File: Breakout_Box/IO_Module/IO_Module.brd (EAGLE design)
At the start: 64 x 35 mm, 5 parts, among them U1 AGND, U2 AGND, U3 AGND

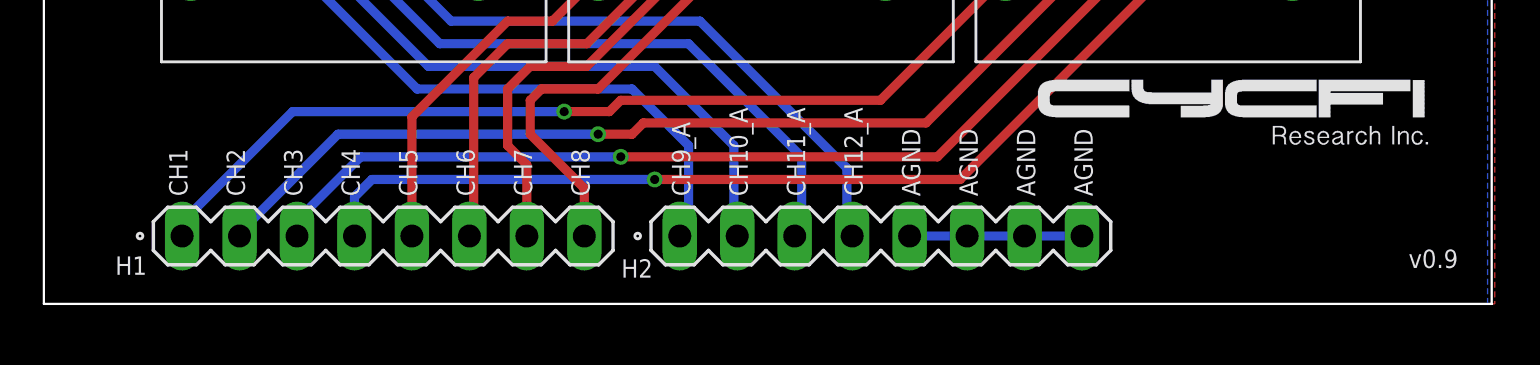
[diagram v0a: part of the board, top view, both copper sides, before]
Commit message: Update: Main Board MIDI Board MCU Board IO Board
Delete:
Mixer Board
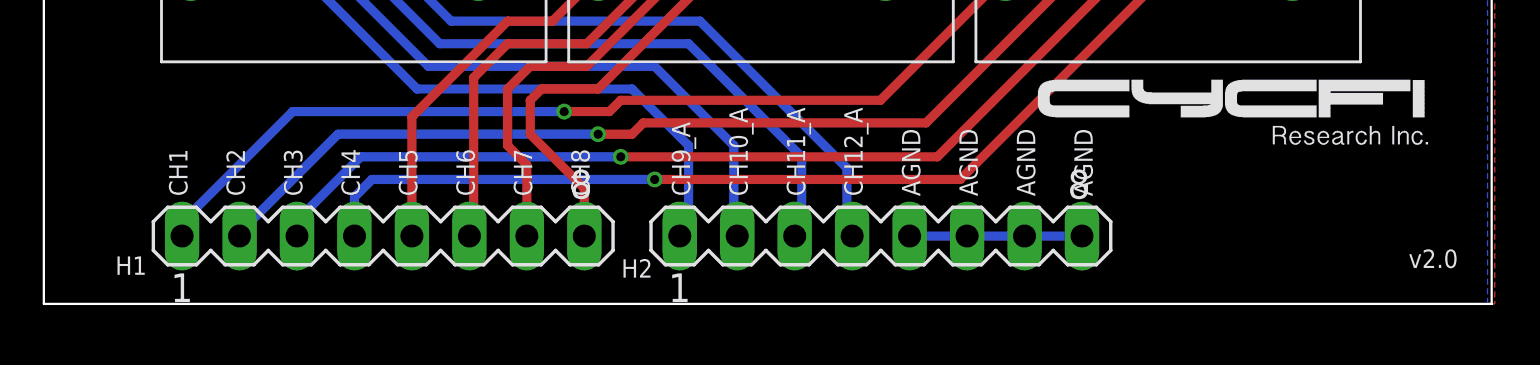
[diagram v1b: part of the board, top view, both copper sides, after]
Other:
- board text added: "v2.0"
- board text removed: "v0.9"
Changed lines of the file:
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@@
 <?xml version="1.0" encoding="utf-8"?>
 <!DOCTYPE eagle SYSTEM "eagle.dtd">
-<eagle version="6.3">
+<eagle version="9.0.0">
 <drawing>
 <settings>
-<setting alwaysvectorfont="yes"/>
+<setting alwaysvectorfont="no"/>
+<setting keepoldvectorfont="yes"/>
 <setting verticaltext="up"/>
 </settings>
@@
 <layer number="59" name="tCarbon" color="7" fill="1" visible="no" active="no"/>
 <layer number="60" name="bCarbon" color="7" fill="1" visible="no" active="no"/>
-<layer number="90" name="Modules" color="5" fill="1" visible="yes" active="yes"/>
+<layer number="90" name="Modules" color="5" fill="1" visible="no" active="no"/>
 <layer number="91" name="Nets" color="2" fill="1" visible="no" active="no"/>
 <layer number="92" name="Busses" color="1" fill="1" visible="no" active="no"/>
@@
 <text x="43.8242" y="4.7611" size="0.8128" layer="25" ratio="10" rot="R90">AGND</text>
 <text x="46.3642" y="4.7611" size="0.8128" layer="25" ratio="10" rot="R90">AGND</text>
-<text x="60.325" y="1.5875" size="0.8128" layer="25" ratio="10">v0.9</text>
+<text x="60.325" y="1.5875" size="0.8128" layer="25" ratio="10">v2.0</text>
 <rectangle x1="55.249190625" y1="7.03266875" x2="55.391428125" y2="7.05045" layer="25"/>
 <rectangle x1="55.853709375" y1="7.03266875" x2="56.013728125" y2="7.05045" layer="25"/>
@@
 <text x="43.8242" y="4.7611" size="0.8128" layer="125" ratio="10" rot="R90">AGND</text>
 <text x="46.3642" y="4.7611" size="0.8128" layer="125" ratio="10" rot="R90">AGND</text>
-<text x="60.325" y="1.5875" size="0.8128" layer="125" ratio="10">v0.9</text>
+<text x="60.325" y="1.5875" size="0.8128" layer="125" ratio="10">v2.0</text>
 <rectangle x1="55.249190625" y1="7.03266875" x2="55.391428125" y2="7.05045" layer="125"/>
 <rectangle x1="55.853709375" y1="7.03266875" x2="56.013728125" y2="7.05045" layer="125"/>
@@
 <param name="dpMaxLengthDifference" value="10mm"/>
 <param name="dpGapFactor" value="2.5"/>
-<param name="checkGrid" value="0"/>
 <param name="checkAngle" value="0"/>
 <param name="checkFont" value="1"/>
 <param name="checkRestrict" value="0"/>
+<param name="checkStop" value="0"/>
+<param name="checkValues" value="0"/>
 <param name="useDiameter" value="13"/>
 <param name="maxErrors" value="50"/>
@@
 <pass name="Default">
 <param name="RoutingGrid" value="50mil"/>
+<param name="AutoGrid" value="1"/>
+<param name="Efforts" value="0"/>
+<param name="TopRouterVariant" value="1"/>
 <param name="tpViaShape" value="round"/>
 <param name="PrefDir.1" value="|"/>
@@
 </autorouter>
 <elements>
-<element name="H2" library="con-lstb" package="MA08-1" value="" x="37" y="3" smashed="yes">
+<element name="H2" library="con-lstb" library_urn="urn:adsk.eagle:library:162" package="MA08-1" package3d_urn="urn:adsk.eagle:package:8343/1" value="" x="37" y="3" smashed="yes">
+<attribute name="MF" value="" x="61.13" y="-54.15" size="1.778" layer="27" display="off"/>
+<attribute name="MPN" value="" x="61.13" y="-54.15" size="1.778" layer="27" display="off"/>
+<attribute name="NAME" x="25.5225" y="1.1585" size="0.8128" layer="25" ratio="10"/>
+<attribute name="OC_FARNELL" value="unknown" x="61.13" y="-54.15" size="1.778" layer="27" display="off"/>
 <attribute name="OC_NEWARK" value="unknown" x="61.13" y="-54.15" size="1.778" layer="27" display="off"/>
-<attribute name="MPN" value="" x="61.13" y="-54.15" size="1.778" layer="27" display="off"/>
-<attribute name="MF" value="" x="61.13" y="-54.15" size="1.778" layer="27" display="off"/>
-<attribute name="OC_FARNELL" value="unknown" x="61.13" y="-54.15" size="1.778" layer="27" display="off"/>
-<attribute name="NAME" x="25.5225" y="1.1585" size="0.8128" layer="25" ratio="10"/>
 <attribute name="VALUE" x="35.73" y="0.079" size="1.27" layer="27" ratio="10"/>
 </element>
-<element name="H1" library="con-lstb" package="MA08-1" value="" x="15" y="3" smashed="yes">
+<element name="H1" library="con-lstb" library_urn="urn:adsk.eagle:library:162" package="MA08-1" package3d_urn="urn:adsk.eagle:package:8343/1" value="" x="15" y="3" smashed="yes">
+<attribute name="MF" value="" x="60.72" y="-54.15" size="1.778" layer="27" display="off"/>
+<attribute name="MPN" value="" x="60.72" y="-54.15" size="1.778" layer="27" display="off"/>
+<attribute name="NAME" x="3.1575" y="1.286" size="0.8128" layer="25" ratio="10"/>
+<attribute name="OC_FARNELL" value="unknown" x="60.72" y="-54.15" size="1.778" layer="27" display="off"/>
 <attribute name="OC_NEWARK" value="unknown" x="60.72" y="-54.15" size="1.778" layer="27" display="off"/>
-<attribute name="MPN" value="" x="60.72" y="-54.15" size="1.778" layer="27" display="off"/>
-<attribute name="MF" value="" x="60.72" y="-54.15" size="1.778" layer="27" display="off"/>
-<attribute name="OC_FARNELL" value="unknown" x="60.72" y="-54.15" size="1.778" layer="27" display="off"/>
-<attribute name="NAME" x="3.1575" y="1.286" size="0.8128" layer="25" ratio="10"/>
 <attribute name="VALUE" x="13.73" y="0.079" size="1.27" layer="27" ratio="10"/>
 </element>
@@
 </board>
 </drawing>
+<compatibility>
+<note version="8.2" severity="warning">
+Since Version 8.2, EAGLE supports online libraries. The ids
+of those online libraries will not be understood (or retained)
+with this version.
+</note>
+<note version="8.3" severity="warning">
+Since Version 8.3, EAGLE supports URNs for individual library
+assets (packages, symbols, and devices). The URNs of those assets
+will not be understood (or retained) with this version.
+</note>
+<note version="8.3" severity="warning">
+Since Version 8.3, EAGLE supports the association of 3D packages
+with devices in libraries, schematics, and board files. Those 3D
+packages will not be understood (or retained) with this version.
+</note>
+</compatibility>
 </eagle>
